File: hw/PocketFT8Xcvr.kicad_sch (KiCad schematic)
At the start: 55 parts, among them J1 HX8357D, J2 ANT, J3 +12V, J4 Conn_01x07, Q1 2N3904, Q2 2N3906, Q3 2N7000, Q4 2N7000, U1 MCP3422A1T-E/SN, U2 Si4735-D60-GU, U3 GVA-84+, U4 L7805CV

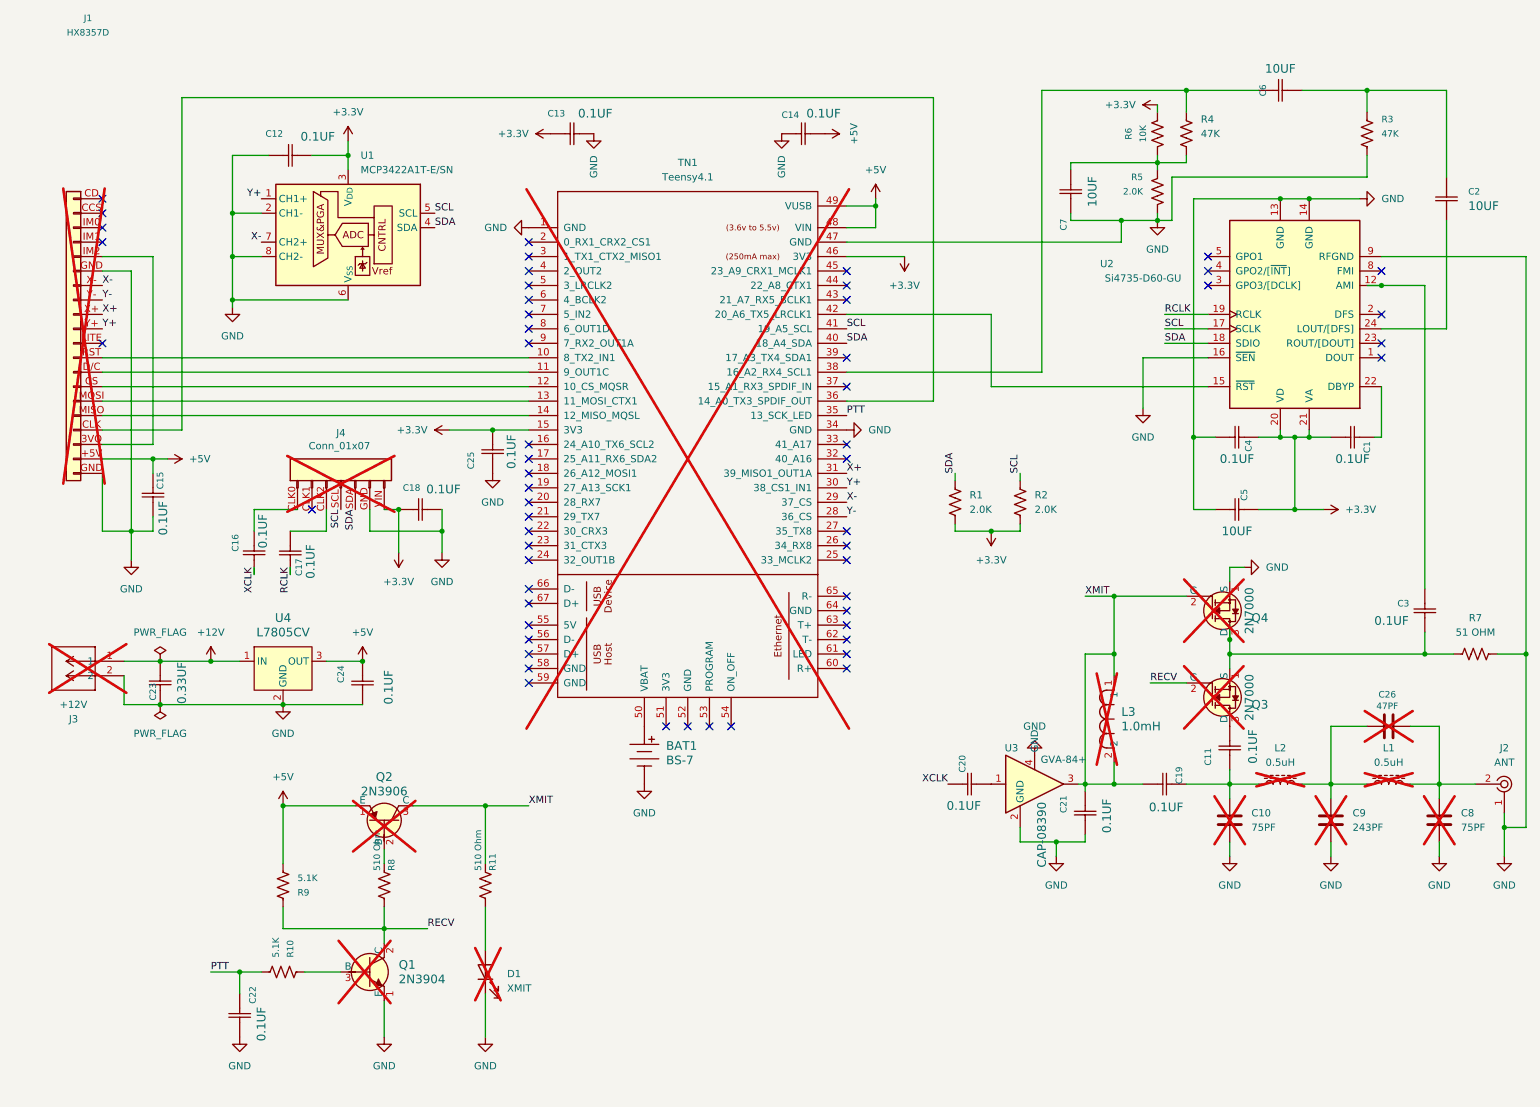
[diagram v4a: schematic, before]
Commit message: Re-run ERC after assembling the BOM
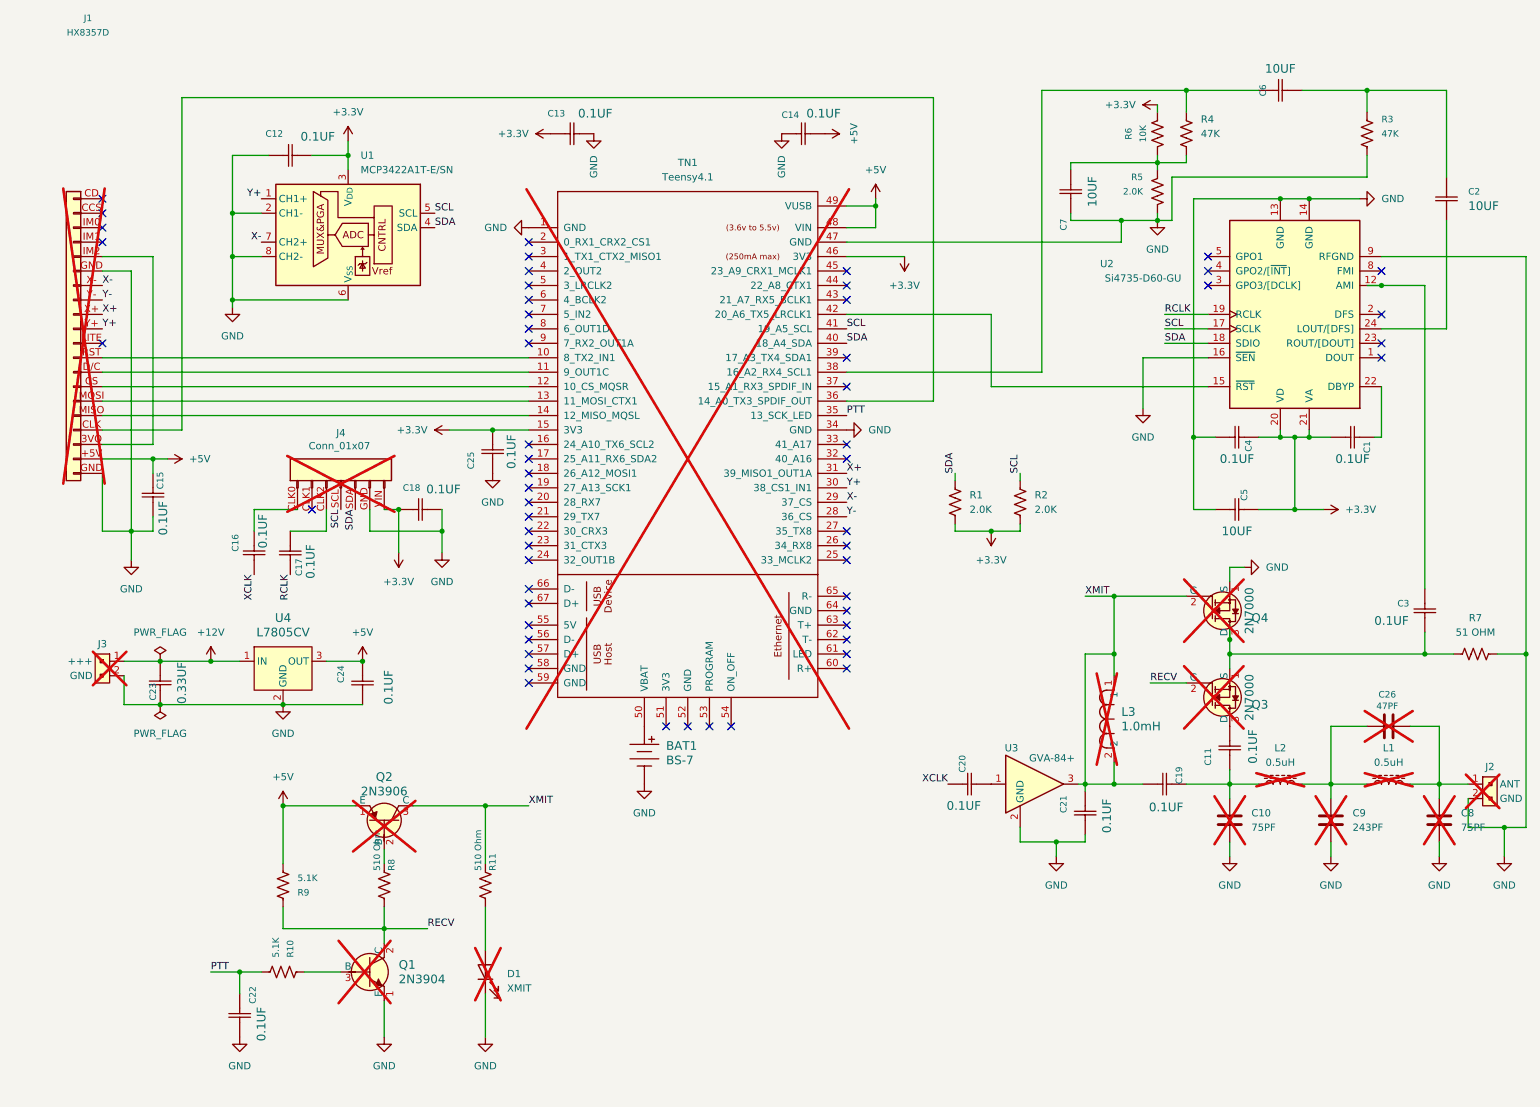
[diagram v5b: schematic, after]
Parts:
- removed J2: ANT, digikey-footprints:RF_SMA_RightAngle_5-1814400-1, symbol dk_Coaxial-Connectors-RF:5-1814400-1
- removed J3: +12V, CONN1x2_PJ-037A_CUD, symbol BarrelJackTHT:PJ-037A
- added J2, J3: 22-23-2021, digikey-footprints:PinHeader_1x2_P2.54mm_Drill1.02mm, symbol dk_Rectangular-Connectors-Headers-Male-Pins:22-23-2021
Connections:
- net +12V: now also J3.1 (+++)
- net GND: now also J2.2 (GND), J3.2 (GND)
- net at C26.2, C8.1, L1.2: now also J2.1 (ANT)

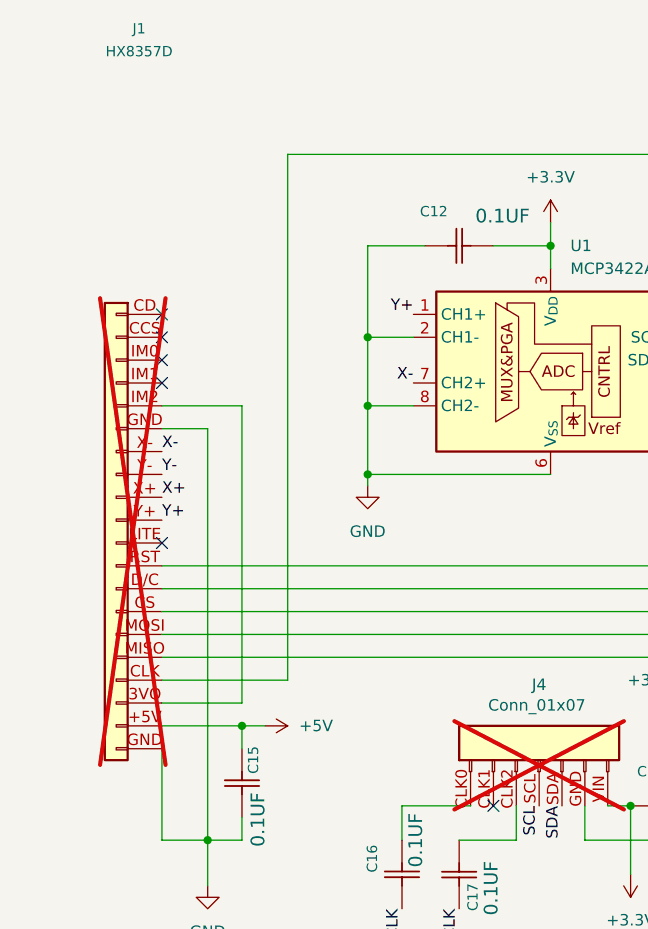
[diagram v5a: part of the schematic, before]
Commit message: Cleanup footprints
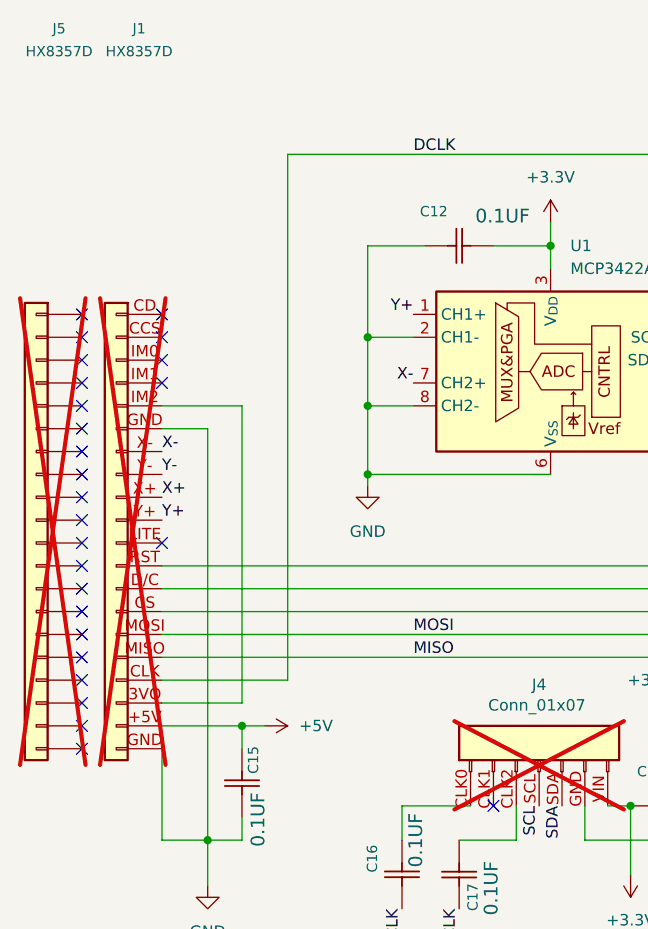
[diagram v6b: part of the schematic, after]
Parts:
- added J5: HX8357D, Connector_PinHeader_2.54mm:PinHeader_1x20_P2.54mm_Vertical, symbol SparkFun-Connector:Conn_01x20
- BAT1: footprint digikey-footprints:Battery_Holder_Coin_2032_BS-7 -> BS-7:BS-7_MPD
- C1, C11, C12, C13, C14, C15, C16, C17, C18, C19, C20, C21, C22, C24, C25, C3, C4: footprint 0603 -> Capacitor_SMD:C_0603_1608Metric
- C10, C2, C26, C5, C6, C7, C8, C9: footprint 0805 -> Capacitor_SMD:C_0805_2012Metric
- J1: footprint SparkFun-Connector:1x20 -> Connector_PinHeader_2.54mm:PinHeader_1x20_P2.54mm_Vertical
- J4: footprint SparkFun-Connector:1x07 -> Connector_PinHeader_2.54mm:PinHeader_1x07_P2.54mm_Vertical
- R1, R10, R11, R2, R3, R4, R5, R6, R7, R8, R9: footprint 0603 -> Resistor_SMD:R_0603_1608Metric
- TN1: footprint (none) -> teensy:Teensy41
- U3: footprint SOT-89-4 -> Package_TO_SOT_SMD:SOT-89-3_Handsoldering; Notes (none) -> hand soldering footprint used for better heat sink
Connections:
- net DCLK: now reaches J1.CLK (Pin_17), TN1.36 (14_A0_TX3_SPDIF_OUT)
- net MISO: now reaches J1.MISO, TN1.14 (12_MISO_MQSL)
- net MOSI: now reaches J1.MOSI (Pin_15), TN1.13 (11_MOSI_CTX1)
- no-connect marks 57 -> 77

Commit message: Imported components to PCB
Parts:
- BAT1: value BS-7 -> BU2032SM-JJ-GTR; footprint BS-7:BS-7_MPD -> BU2032SM-JJ-GTR_MPD; symbol dk_Battery-Holders-Clips-Contacts:BS-7 -> 2024-08-05_00-31-14:BU2032SM-JJ-GTR; DK_Datasheet_Link http://www.memoryprotectiondevices.com/datasheets/BS-7-data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 -> (none); DK_Detail_Page /product-detail/en/mpd-memory-protection-devices/BS-7/BS-7-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 -> (none); Digi-Key_PN BS-7-ND -> (none); Mfg Part # BS-7 -> BU2032SM-JJ-GTR; Notes (none) -> Must mount topside
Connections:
- net GND: now also BAT1.1; no longer BAT1.Neg
- net at TN1.50 (VBAT): now also BAT1.2; no longer BAT1.Pos
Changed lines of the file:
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@@
 	)
 	(symbol
-		(lib_id "dk_Battery-Holders-Clips-Contacts:BS-7")
-		(at 124.46 137.16 0)
+		(lib_id "2024-08-05_00-31-14:BU2032SM-JJ-GTR")
+		(at 124.46 132.08 270)
 		(unit 1)
 		(exclude_from_sim no)
@@
 		(fields_autoplaced yes)
 		(property "Reference" "BAT1"
-			(at 128.27 135.509 0)
+			(at 127 135.8899 90)
 			(effects
 				(font
@@
 			)
 		)
-		(property "Value" "BS-7"
-			(at 128.27 138.049 0)
+		(property "Value" "BU2032SM-JJ-GTR"
+			(at 127 138.4299 90)
 			(effects
 				(font
@@
 			)
 		)
-		(property "Footprint" "BS-7:BS-7_MPD"
-			(at 129.54 132.08 0)
+		(property "Footprint" "BU2032SM-JJ-GTR_MPD"
+			(at 124.46 132.08 0)
 			(effects
 				(font
-					(size 1.524 1.524)
+					(size 1.27 1.27)
+					(italic yes)
 				)
-				(justify left)
 				(hide yes)
 			)
 		)
-		(property "Datasheet" "http://www.memoryprotectiondevices.com/datasheets/BS-7-datasheet.pdf"
-			(at 129.54 129.54 90)
+		(property "Datasheet" "BU2032SM-JJ-GTR"
+			(at 124.46 132.08 0)
 			(effects
 				(font
-					(size 1.524 1.524)
+					(size 1.27 1.27)
+					(italic yes)
 				)
-				(justify left)
 				(hide yes)
 			)
 		)
-		(property "Description" "BATTERY HOLDER COIN 20MM PC PIN"
-			(at 129.54 111.76 0)
+		(property "Description" "BATT HOLDER COIN 20MM 1 CELL SMD"
+			(at 124.46 132.08 0)
 			(effects
 				(font
-					(size 1.524 1.524)
+					(size 1.27 1.27)
 				)
-				(justify left)
 				(hide yes)
 			)
 		)
-		(property "Digi-Key_PN" "BS-7-ND"
-			(at 129.54 127 0)
-			(effects
-				(font
-					(size 1.524 1.524)
-				)
-				(justify left)
-				(hide yes)
-			)
-		)
-		(property "Mfg Part #" "BS-7"
-			(at 129.54 124.46 0)
+		(property "Mfg Part #" "BU2032SM-JJ-GTR"
+			(at 137.16 137.16 0)
 			(effects
 				(font
@@
 		)
 		(property "Category" "Battery Products"
-			(at 129.54 121.92 0)
+			(at 139.7 137.16 0)
 			(effects
 				(font
@@
 		)
 		(property "Family" "Battery Holders, Clips, Contacts"
-			(at 129.54 119.38 0)
-			(effects
-				(font
-					(size 1.524 1.524)
-				)
-				(justify left)
-				(hide yes)
-			)
-		)
-		(property "DK_Datasheet_Link" "http://www.memoryprotectiondevices.com/datasheets/BS-7-datasheet.pdf"
-			(at 129.54 116.84 0)
-			(effects
-				(font
-					(size 1.524 1.524)
-				)
-				(justify left)
-				(hide yes)
-			)
-		)
-		(property "DK_Detail_Page" "/product-detail/en/mpd-memory-protection-devices/BS-7/BS-7-ND/389447"
-			(at 129.54 114.3 0)
+			(at 142.24 137.16 0)
 			(effects
 				(font
@@
 		)
 		(property "Manufacturer" "MPD (Memory Protection Devices)"
-			(at 129.54 109.22 0)
+			(at 152.4 137.16 0)
 			(effects
 				(font
@@
 		)
 		(property "Status" "Active"
-			(at 129.54 106.68 0)
+			(at 154.94 137.16 0)
 			(effects
 				(font
@@
 		)
 		(property "Description_1" "BATTERY HOLDER COIN 20MM PC PIN"
-			(at 129.54 111.76 0)
+			(at 149.86 137.16 0)
 			(effects
 				(font
@@
 		)
 		(property "Type" "SMD"
-			(at 124.46 137.16 0)
+			(at 124.46 132.08 0)
 			(effects
 				(font
@@
 			)
 		)
-		(property "Notes" ""
-			(at 124.46 137.16 0)
+		(property "Notes" "Must mount topside"
+			(at 124.46 132.08 0)
 			(effects
 				(font
@@
 			)
 		)
-		(pin "Neg"
+		(pin "1"
 		)
-		(pin "Pos"
+		(pin "2"
 		)
 		(instances

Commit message: Begin populating board
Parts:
- removed C16, C17, C18, C21: 0.1UF, Capacitor_SMD:C_0603_1608Metric, symbol Kemet2024-08-02_22-05-35:C0603C104K4RACTU
- removed J4: Conn_01x07, Connector_PinHeader_2.54mm:PinHeader_1x07_P2.54mm_Vertical, symbol SparkFun-Connector:Conn_01x07
- added C27, C28, C29, C30: 0.1UF, Capacitor_SMD:C_0603_1608Metric, symbol Kemet2024-08-02_22-05-35:C0603C104K4RACTU
- added IC1: SI5351C-B-GM1, SI5351C-B-GM1:QFN50P300X300X90-17N-D, symbol SI5351C-B-GM1:SI5351C-B-GM1
- added Y1: ASTX-H11-25.000MHZ-T, ASTX_H11_25_000MHZ_T:XTAL_ASTX-H11-25.000MHZ-T, symbol ASTX-H11-25.000MHZ-T:ASTX-H11-25.000MHZ-T
- J1: value HX8357D -> HX8357D SPI
- J5: value HX8357D -> HX8357D 8-BIT
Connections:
- net +3.3V: now also C27.2, Y1.4 (VDD)
- net +5V: now also J1.19 (Vin); no longer J1.+5V (Pin_19)
- net DCLK: now also J1.17 (CLK); no longer J1.CLK (Pin_17)
- net GND: now also J1.20 (GND), J1.6 (GND), C27.1, C28.2, C29.1, C30.1, IC1.15 (GND_1), IC1.17 (GND_2), IC1.3 (OEB), Y1.2 (GND); no longer J1.GND (Pin_6)
- net MISO: now also J1.16 (MISO); no longer J1.MISO
- net MOSI: now also J1.15 (MOSI); no longer J1.MOSI (Pin_15)
- net RCLK: now also IC1.13 (CLK2)
- net SCL: now also IC1.4 (SCL)
- net SDA: now also IC1.5 (SDA)
- net X+: now also J1.9 (X+); no longer J1.X+ (Pin_9)
- net X-: now also J1.7 (X-); no longer J1.X- (Pin_7)
- net XCLK: now also IC1.10 (CLK0)
- net XMIT: no longer C19.1, L3.2, U3.3
- net Y+: now also J1.10 (Y+); no longer J1.Y+ (Pin_10)
- net Y-: now also J1.8 (Y-); no longer J1.Y- (Pin_8)
- net at TN1.12 (10_CS_MQSR): now also J1.14 (CS); no longer J1.CS (Pin_14)
- net at TN1.11 (9_OUT1C): now also J1.13 (D/C); no longer J1.D/C (Pin_13)
- net at TN1.10 (8_TX2_IN1): now also J1.12 (RST); no longer J1.RST (Pin_12)
- new net: C19.1, L3.2, U3.3
- new net: C28.1, C29.2, C30.2, IC1.11 (VDDOD), IC1.14 (VDDOC), IC1.16 (VDD), IC1.8 (VDDOB), IC1.9 (VDDOA)
- new net: IC1.6 (CLKIN), Y1.3 (OUTPUT)
- new net: J1.18 (3Vo), J1.5 (IM2)
- no-connect marks 77 -> 81
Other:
- moved on the sheet: C22, D1, Q1, Q2, R10, R11, R8, R9
